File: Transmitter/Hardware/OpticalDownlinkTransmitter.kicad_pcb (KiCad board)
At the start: 2 copper layers, 84 x 84 mm, 34 parts, among them J1 Conn_01x04_Pin, J2 Conn_01x04_Pin, U1 AL8860MP, U2 AL8860MP, U3 AL8860MP, U4 AL8860MP

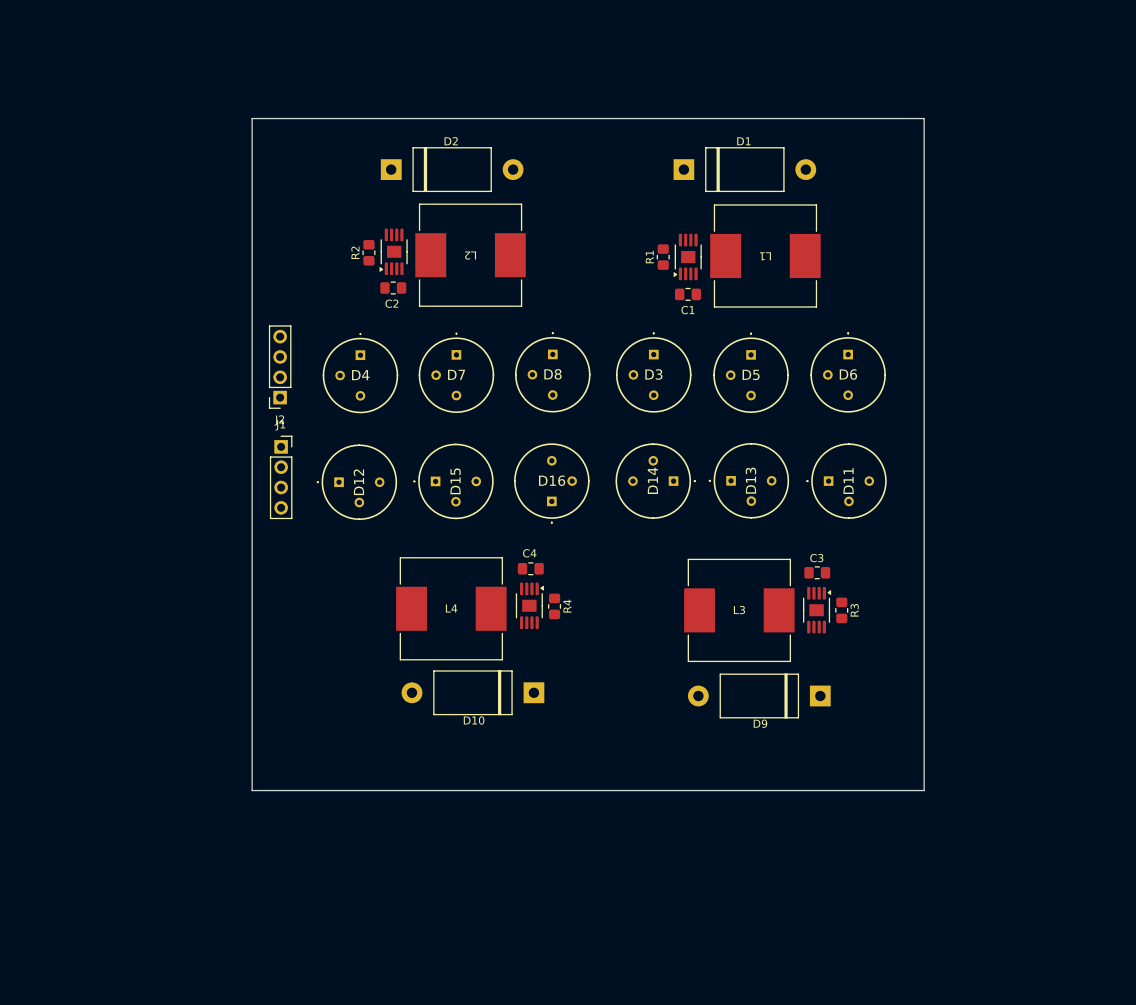
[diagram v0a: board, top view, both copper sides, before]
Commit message: added footprints and redid layout
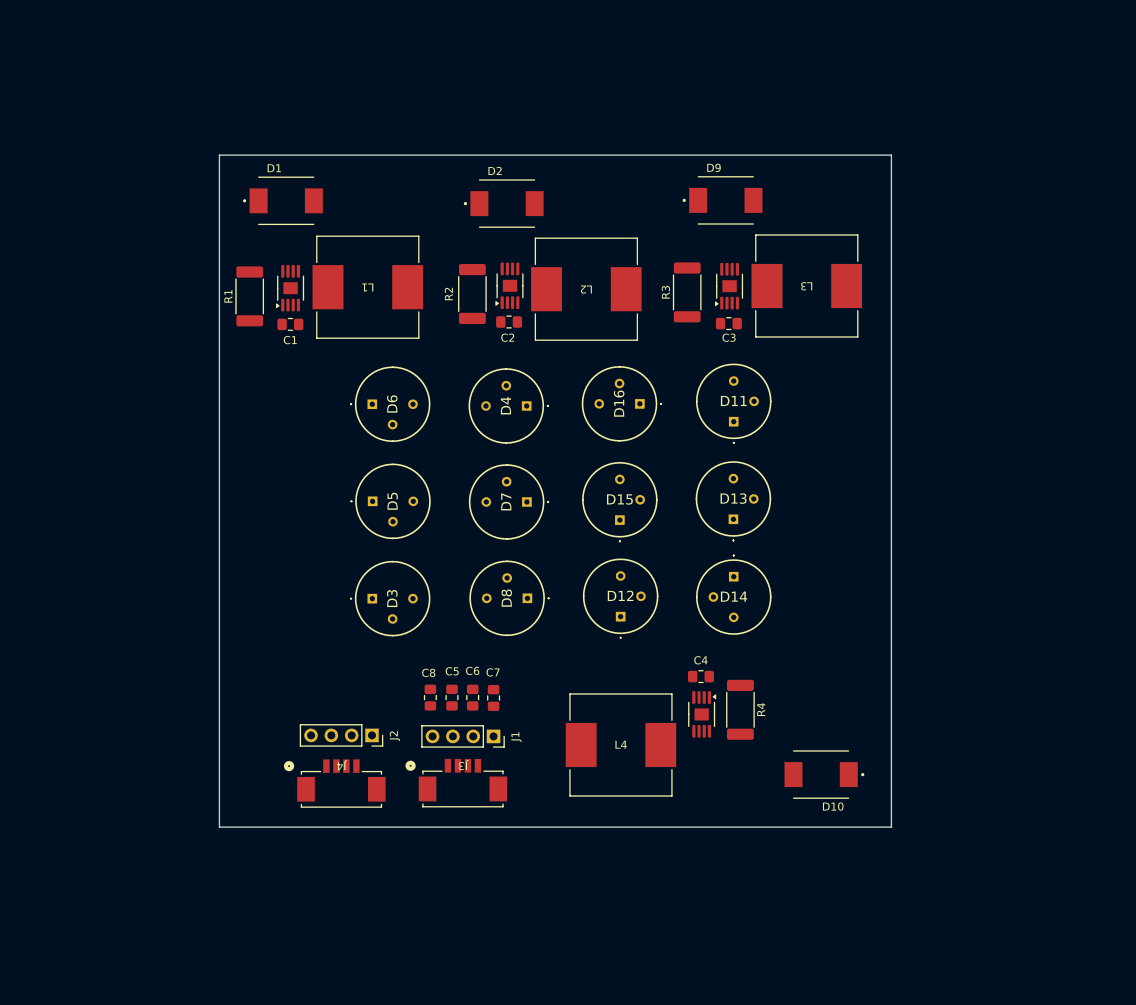
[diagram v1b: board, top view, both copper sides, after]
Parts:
- added C5: 10uF, Capacitor_SMD:C_0805_2012Metric_Pad1.18x1.45mm_HandSolder, F.Cu at (133.1, 118.4)
- added C6: 10uF, Capacitor_SMD:C_0805_2012Metric_Pad1.18x1.45mm_HandSolder, F.Cu at (135.7, 118.4)
- added C7: 10uF, Capacitor_SMD:C_0805_2012Metric_Pad1.18x1.45mm_HandSolder, F.Cu at (138.3, 118.5)
- added C8: 10uF, Capacitor_SMD:C_0805_2012Metric_Pad1.18x1.45mm_HandSolder, F.Cu at (130.4, 118.4)
- added J3: Conn_01x04, Footprint Library:CONN_532610001-SD_04_MOL, F.Cu at (134.4, 129.8)
- added J4: Conn_01x04, Footprint Library:CONN_532610001-SD_04_MOL, F.Cu at (119.3, 129.9)
- D1, D10, D2, D9: footprint Footprint Library:P2_DO-201 -> Footprint Library:DIOM7959X261N
- L1, L2, L3, L4: value 50uH -> 47uH
- R1, R2, R3, R4: value 0.285Ω -> 0.250Ω; footprint Resistor_SMD:R_0805_2012Metric_Pad1.20x1.40mm_HandSolder -> Resistor_SMD:R_2512_6332Metric_Pad1.40x3.35mm_HandSolder
- moved D9 63.1 mm to (167.3, 56.2), turned to 0 degrees
- moved D6 59.8 mm to (123.1, 81.7), turned to 90 degrees
- moved R1 51.9 mm to (107.8, 68.2)
- moved D5 50.7 mm to (123.2, 93.9), turned to 90 degrees
- moved D1 49.9 mm to (112.4, 56.3)
- moved L1 49.9 mm to (122.6, 67.1)
- moved U1 49.9 mm to (112.9, 67.2)
- moved C1 49.8 mm to (112.9, 71.8)
- moved D3 46.6 mm to (123.1, 106.0), turned to 90 degrees
- moved J1 44.9 mm to (138.3, 123.2), turned to -90 degrees
- moved R3 44.2 mm to (162.5, 67.8), turned to 90 degrees
- moved J2 43.8 mm to (123.1, 123.1), turned to -90 degrees
- moved U3 41.9 mm to (167.8, 67.0), turned to 90 degrees
- moved L3 41.4 mm to (177.4, 67.0), turned to 180 degrees
- moved D12 39.0 mm to (154.2, 108.3), turned to 180 degrees
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
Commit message: Adjusted layout so tracing would be easier
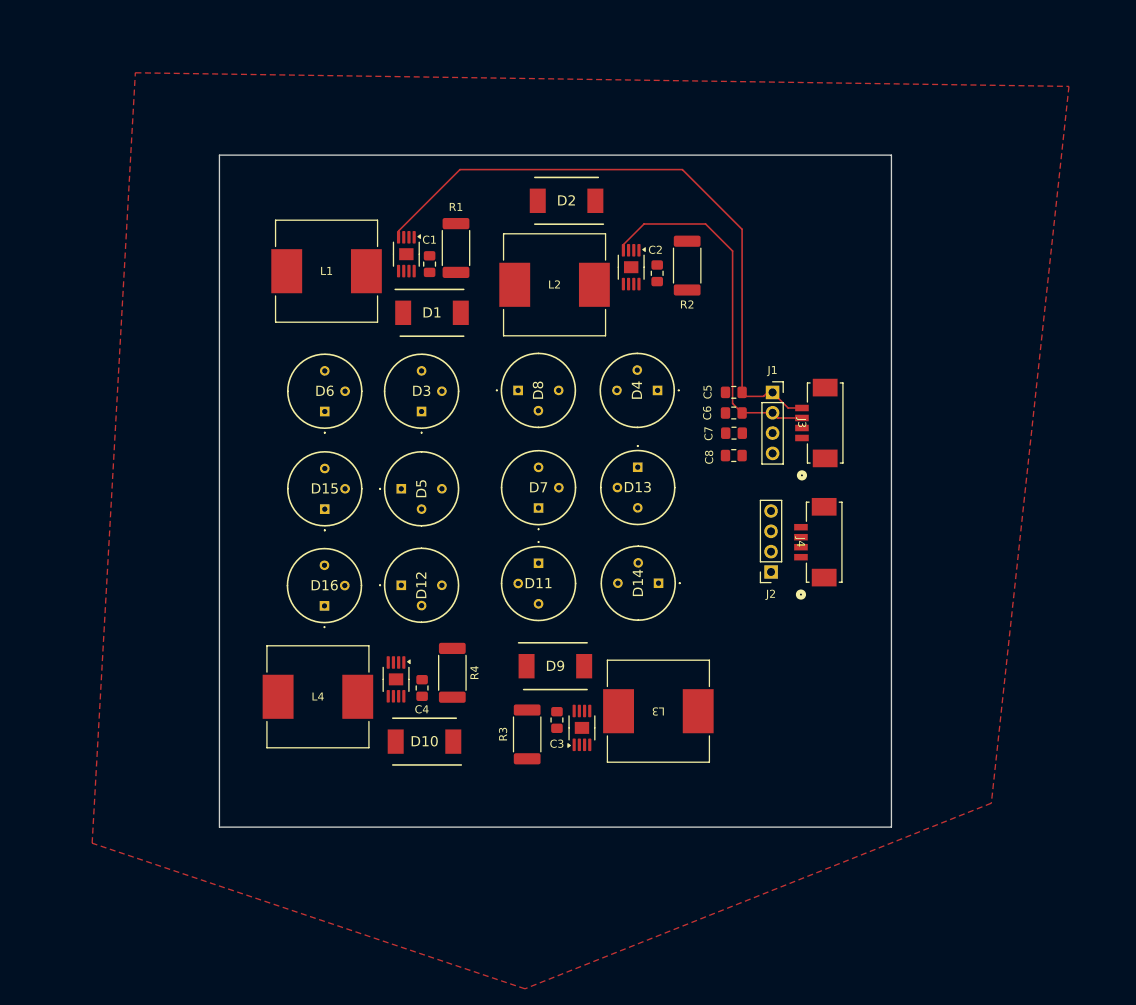
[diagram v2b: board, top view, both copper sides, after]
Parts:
- D1, D10, D2, D9: footprint Footprint Library:DIOM7959X261N -> Footprint Library:DIOM7958X256N
- moved J4 67.8 mm to (179.6, 99.0), turned to -90 degrees
- moved J3 64.4 mm to (179.7, 84.1), turned to -90 degrees
- moved D9 62.0 mm to (146.0, 114.5)
- moved R3 58.8 mm to (142.5, 123.0)
- moved U3 58.2 mm to (149.3, 122.2)
- moved L3 56.3 mm to (158.9, 120.1)
- moved J1 55.4 mm to (173.2, 80.3), turned to 0 degrees
- moved C3 54.0 mm to (146.2, 121.2), turned to -90 degrees
- moved J2 53.9 mm to (173.0, 102.7), turned to 180 degrees
- moved C5 51.9 mm to (168.3, 80.2), turned to 180 degrees
- moved D10 49.7 mm to (129.6, 123.9)
- moved C8 48.5 mm to (168.3, 88.1), turned to 180 degrees
- moved C6 48.3 mm to (168.3, 82.8), turned to 180 degrees
- moved D16 46.8 mm to (117.1, 106.9), turned to 180 degrees
- moved C7 44.7 mm to (168.3, 85.3), turned to 180 degrees
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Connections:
- J2 pad 1: V_{DD} -> 12V
- J2 pad 2: V_{DD} -> 12V
- J2 pad 3: V_{DD} -> 12V
- J4 pad 1: V_{DD} -> 12V
- J4 pad 2: V_{DD} -> 12V
- J4 pad 3: V_{DD} -> 12V
- L1 pad 2: Net-(D1-A) -> Net-(D1-K)
- U1 pad 5: Net-(D1-A) -> Net-(D1-K)
- U1 pad 6: Net-(D1-A) -> Net-(D1-K)
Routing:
- net Ctrl 1: track 0.00 -> 79.1 mm
- net Ctrl 2: track 0.00 -> 45.3 mm
- net Net-(D2-A): track 0.00 -> 0.90 mm
- added copper zone on F.Cu, net 12V

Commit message: traced almost all of the components together and added mounting holes
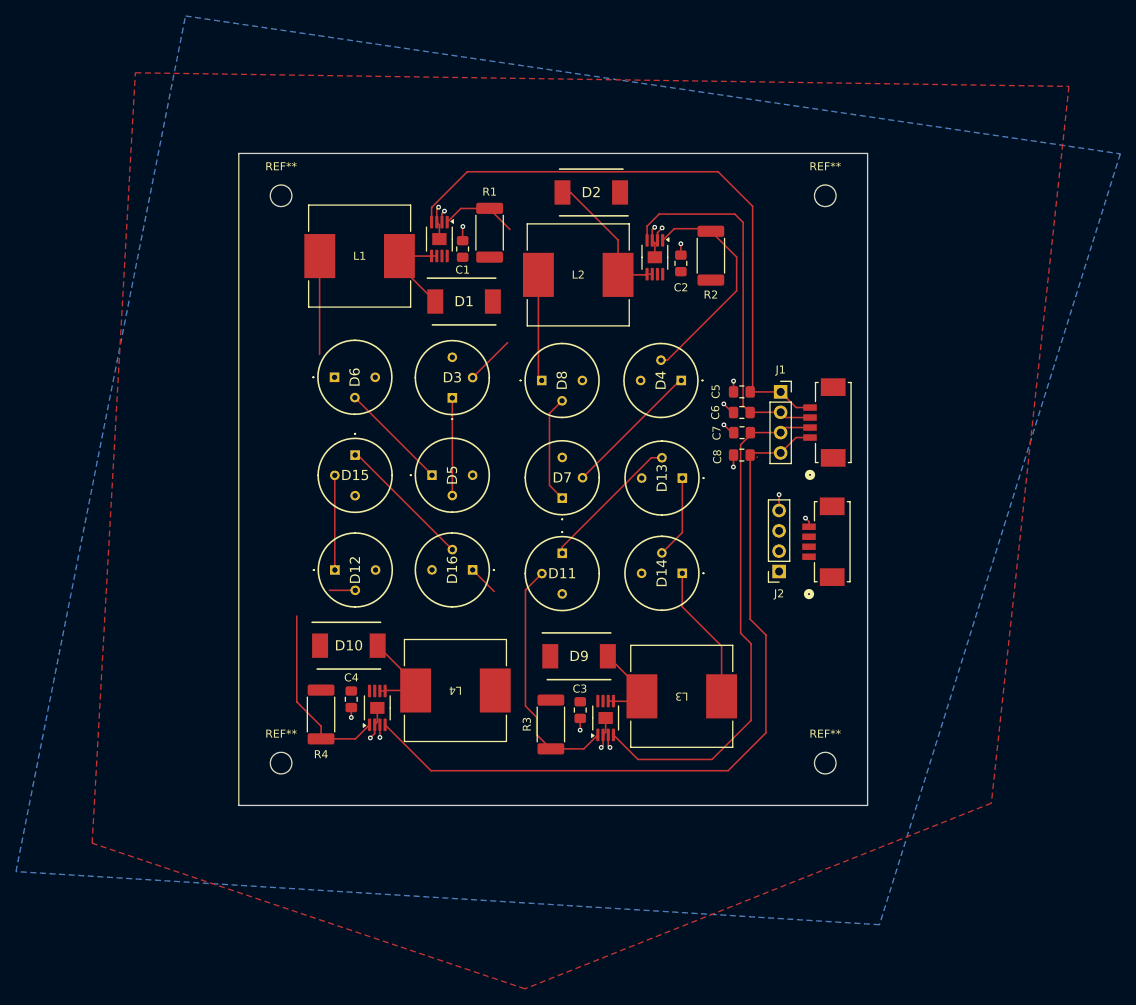
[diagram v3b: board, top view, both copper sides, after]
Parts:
- added REF**: MountingHole_2.7mm_M2.5, MountingHole:MountingHole_2.7mm_M2.5, F.Cu at (179.7, 126.6)
- added REF**: MountingHole_2.7mm_M2.5, MountingHole:MountingHole_2.7mm_M2.5, F.Cu at (179.7, 55.7)
- added REF**: MountingHole_2.7mm_M2.5, MountingHole:MountingHole_2.7mm_M2.5, F.Cu at (111.7, 55.7)
- added REF**: MountingHole_2.7mm_M2.5, MountingHole:MountingHole_2.7mm_M2.5, F.Cu at (111.7, 126.6)
- moved D16 19.1 mm to (135.7, 102.4), turned to -90 degrees
- moved R4 17.2 mm to (116.7, 120.5), turned to 90 degrees
- moved L4 17.2 mm to (133.5, 117.5), turned to 180 degrees
- moved D10 15.3 mm to (120.2, 111.9), turned to 0 degrees
- moved C4 8.97 mm to (120.5, 118.6), turned to -90 degrees
- moved D12 8.50 mm to (118.5, 102.5)
- moved D15 7.75 mm to (121.0, 88.1), turned to 0 degrees
- moved D13 5.74 mm to (161.9, 91.0), turned to -90 degrees
- moved R1 4.62 mm to (137.8, 60.3)
- moved C1 4.54 mm to (134.4, 62.3)
- moved U1 4.54 mm to (131.5, 61.1)
- moved L1 4.54 mm to (121.5, 63.2)
- moved D6 4.45 mm to (118.4, 78.4), turned to 90 degrees
- moved U4 4.27 mm to (123.7, 119.7), turned to 90 degrees
- moved D1 4.25 mm to (134.6, 68.9)
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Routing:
- net Ctrl 4: track 0.00 -> 95.9 mm
- net Ctrl 3: track 0.00 -> 65.2 mm
- net GND: track 0.00 -> 38.0 mm, vias 0 -> 18
- net Net-(D11-A): track 0.00 -> 30.7 mm
- net Net-(D4-A): track 0.00 -> 28.6 mm
- net Net-(D12-A): track 0.00 -> 26.6 mm
- net Net-(D2-A): track 0.90 -> 19.9 mm
- net Net-(D14-K): track 0.00 -> 18.1 mm
- net Net-(D11-K): track 0.00 -> 17.9 mm
- net Net-(D4-K): track 0.00 -> 17.4 mm
- net Net-(D15-K): track 0.00 -> 17.0 mm
- net Net-(D3-A): track 0.00 -> 15.8 mm
- net Net-(D5-K): track 0.00 -> 13.7 mm
- net Net-(D7-K): track 0.00 -> 13.5 mm
- net Net-(D8-K): track 0.00 -> 13.4 mm
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- added copper zone on B.Cu, net GND
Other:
- board size 84 x 84 mm -> 78.6 x 81.5 mm

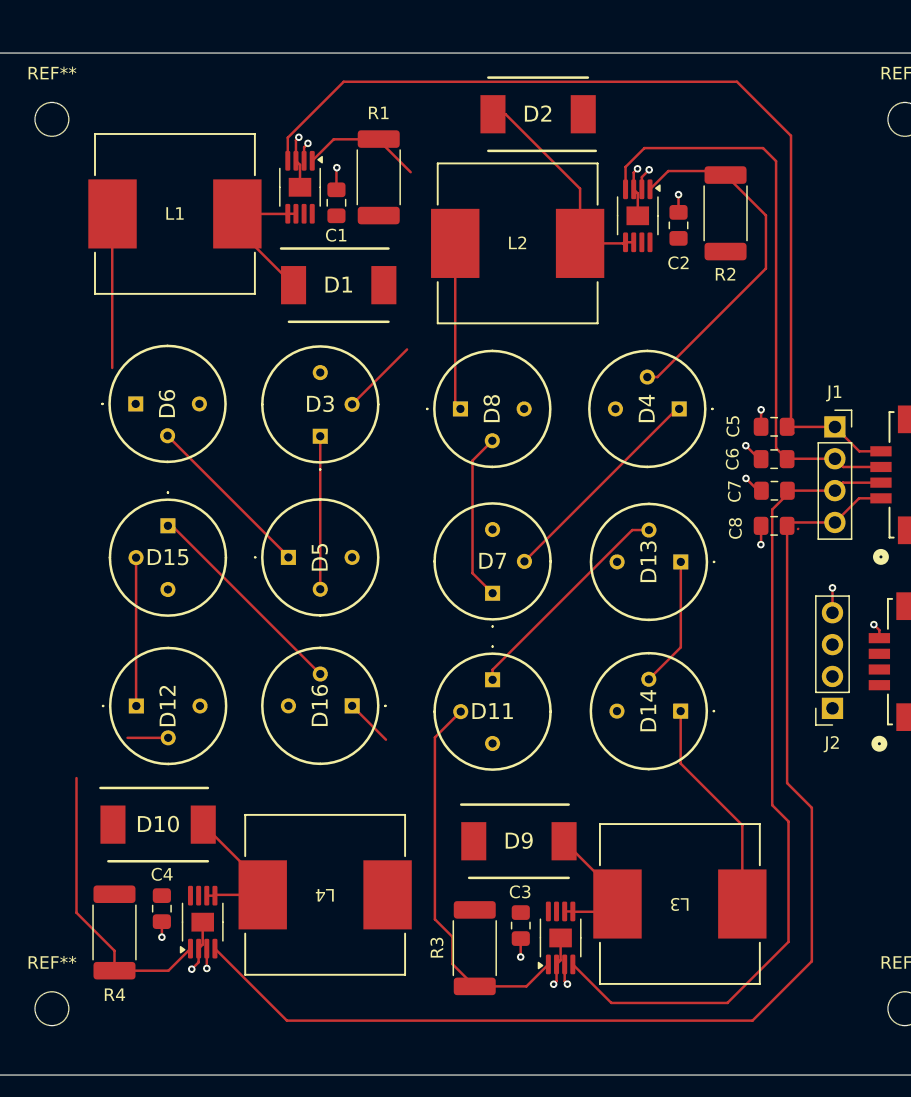
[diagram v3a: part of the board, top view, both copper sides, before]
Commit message: completed tracing and changed polygon clearance and fixed up math in schematic
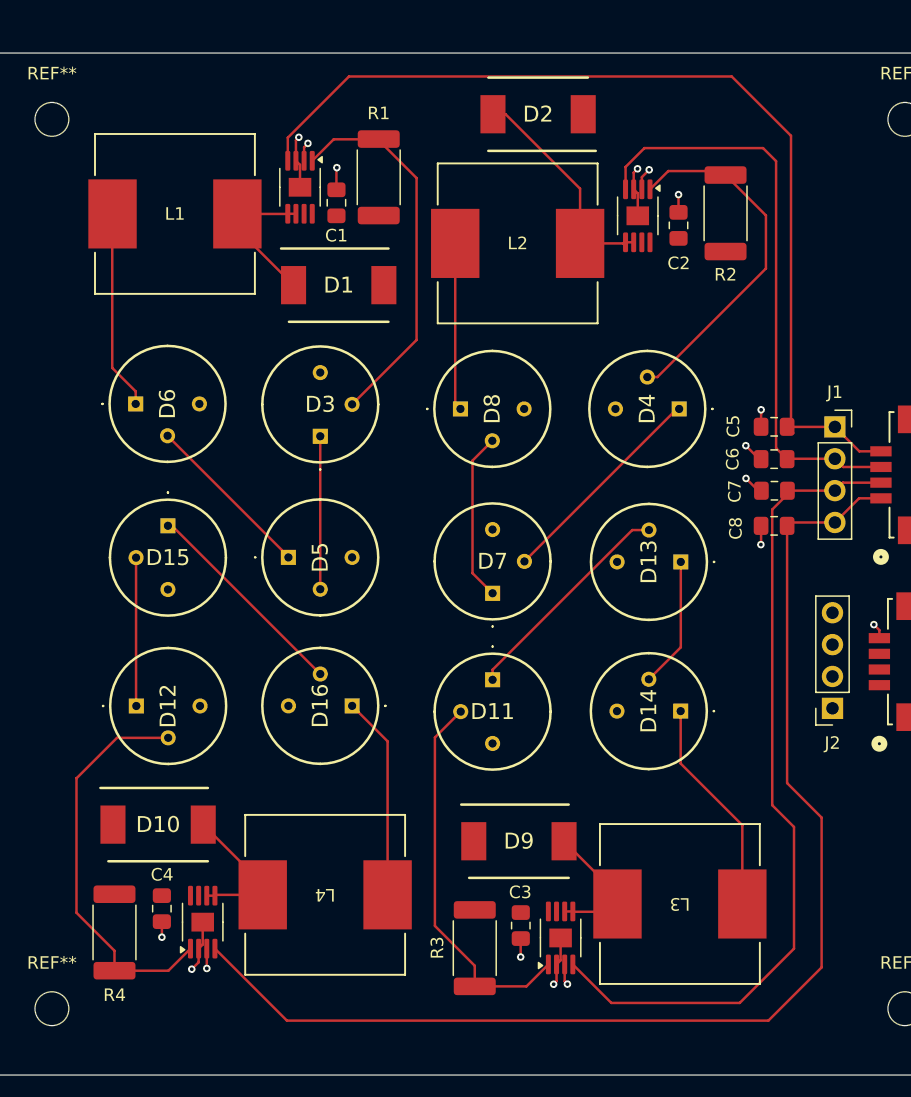
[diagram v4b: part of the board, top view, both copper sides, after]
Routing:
- net Net-(D3-A): track 15.8 -> 30.5 mm
- net Net-(D16-K): track 3.81 -> 16.2 mm
- net Net-(D12-A): track 26.6 -> 32.0 mm
- net Net-(D6-K): track 12.8 -> 16.5 mm
- net GND: track 38.0 -> 36.0 mm, vias 18 -> 17
- net Ctrl 4: track 95.9 -> 97.3 mm
- net Ctrl 3: track 65.2 -> 66.2 mm
